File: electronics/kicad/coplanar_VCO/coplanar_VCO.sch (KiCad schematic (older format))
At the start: 22 parts, among them J1 CONN_01, J2 CONN_01, U1 HMC732, U2 CE3520K3

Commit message: Coplanar
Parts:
- removed C9: 100 nF, 0603, symbol SparkFun-Capacitors:4.7UF0603
- removed C?: 10 nF, 0402, symbol SparkFun-Capacitors:6PF-0402-50V-0.5%
- removed TPOP1: Voutput, TestPoint:TestPoint_Pad_1.0x1.0mm, symbol Connector:Test_Point
- added C10, C14, C15, C20, C24, C25, C29, C9: 0.1 uF, 0603, symbol SparkFun-Capacitors:0.1UF-0603-25V-5%
- added C11, C17, C19, C27, C31, C36, C?: 1 nF, 0402, symbol SparkFun-Capacitors:6PF-0402-50V-0.5%
- added C12, C28, C34: 1 nF, Resistor_SMD:R_0402_1005Metric, symbol SparkFun-Capacitors:4.7UF0603
- added C16, C30, C35, C?: 100 nF, 0603, symbol SparkFun-Capacitors:4.7UF0603
- added C18: 10 nF, 0402, symbol SparkFun-Capacitors:6PF-0402-50V-0.5%
- added C33: 10 nF, Resistor_SMD:R_0402_1005Metric, symbol SparkFun-Capacitors:4.7UF0603
- added C7: 100 pF, 0402, symbol SparkFun-Capacitors:6PF-0402-50V-0.5%
- added D1, D2, D3, D?: BAT15-04, Package_TO_SOT_SMD:SOT-23, symbol Diode:BAS40-04
- added L2: 220 nH, 0402, symbol SparkFun-Coils:INDUCTOR-0402-3.9NH
- added L3: 440 nH, Resistor_SMD:R_0402_1005Metric, symbol SparkFun-Coils:INDUCTOR-0402-3.9NH
- added P1: CONN_1, TestPoint:TestPoint_Pad_1.5x1.5mm, symbol conn:CONN_1
- added P2, P4, P8, P?: a, TestPoint:TestPoint_Pad_1.5x1.5mm, symbol conn:CONN_1
- added P3, P5, P6, P7: OUTPUT, Connector_PinHeader_2.54mm:PinHeader_1x01_P2.54mm_Vertical, symbol conn:CONN_1
- added R11, R13, R4, R8: 100, 0805, symbol SparkFun-Resistors:0.22OHM-0805-1_4W-1%
- added R12, R5: 50, 0805, symbol SparkFun-Resistors:0.22OHM-0805-1_4W-1%
- added R15, R18, R2, R7, R?: 10k, 0402, symbol SparkFun-Resistors:RESISTOR0402
- added R16, R9: 10k, Resistor_SMD:R_0402_1005Metric, symbol SparkFun-Resistors:RESISTOR0402
- added R3: PAT1220, 0xDBFB7:PAT1220, symbol 0xDBFB7:attenuator
- added R? (x4): 1k, Resistor_SMD:R_0603_1608Metric, symbol SparkFun-Resistors:RESISTOR0402
- added U1, U4, U5, U8, U9: SY100EP, Package_SO:SOIC-8_3.9x4.9mm_P1.27mm, symbol 0xDBFB7:SY100EP
- added U10: CE3520K3, 0xDBFB7:4-Micro-X, symbol 0xDBFB7:CE3520K3
- added U3: HMC363, Package_SO:SOIC-8-1EP_3.9x4.9mm_P1.27mm_EP2.35x2.35mm, symbol 0xDBFB7:HMC363
- added U6: SKY65013, Package_TO_SOT_SMD:SOT-89-3_Handsoldering, symbol 0xDBFB7:SKY65013
- C22: renamed from C10; value 1 nF -> 10 nF
- renumbered C8 to C13, C11 to C23, C12 to C26, C7 to C8, R2 to R10, U1 to U2, U2 to U7
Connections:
- net labels added: 3.3V, DIV8_OUT
- wire segments 11 -> 66
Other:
- note added: ""since the detector does not conserve phase information, all phasors that appear as factors can be replaced by their magnitudes." - *happiness noise*"
- note added: "Division of 8 * 4^5 = 8192\n1.464 MHz at 12 GHz."
- note added: "Input power range of the HMC. is max. +5 dBm across the spectrum, 0 dBm recommended.\n"
- note added: "O/P is -9 to -6 dBm, too low for the logic levels of the \nSY."
- note added: "RF diode detector based on infineon appnote AN_1807."
- note added: "Stub lengths < 7 mm probably don't need termination; see Shockman, termination.\nIn fact, the reflection overshoot will aid getting the signal levels between the thresholds."
- note added: "https://www.qsl.net/n9zia/pre1/index.html"
- moved on the sheet: C1, C13, C2, C22, C23, C26, C3, C4, C5, C6, C8, J1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

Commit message: coplanarizing further
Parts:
- removed C1: 10uF, 1206, symbol SparkFun-Capacitors:1.0UF-1206-50V-10%
- removed C10, C14, C15, C20, C24, C25, C29, C3, C9: 0.1 uF, 0603, symbol SparkFun-Capacitors:0.1UF-0603-25V-5%
- removed C11, C17, C19, C27, C36, C?: 1 nF, 0402, symbol SparkFun-Capacitors:6PF-0402-50V-0.5%
- removed C12, C28, C34: 1 nF, Resistor_SMD:R_0402_1005Metric, symbol SparkFun-Capacitors:4.7UF0603
- removed C13, C18: 10 nF, 0402, symbol SparkFun-Capacitors:6PF-0402-50V-0.5%
- removed C16, C35, C?: 100 nF, 0603, symbol SparkFun-Capacitors:4.7UF0603
- removed C26: 10 pF, Capacitor_SMD:C_0402_1005Metric, symbol SparkFun-Capacitors:6PF-0402-50V-0.5%
- removed C33: 10 nF, Resistor_SMD:R_0402_1005Metric, symbol SparkFun-Capacitors:4.7UF0603
- removed C7: 100 pF, 0402, symbol SparkFun-Capacitors:6PF-0402-50V-0.5%
- removed D1, D?: BAT15-04, Package_TO_SOT_SMD:SOT-23, symbol Diode:BAS40-04
- removed L2: 220 nH, 0402, symbol SparkFun-Coils:INDUCTOR-0402-3.9NH
- removed L3: 440 nH, Resistor_SMD:R_0402_1005Metric, symbol SparkFun-Coils:INDUCTOR-0402-3.9NH
- removed P2, P?: a, TestPoint:TestPoint_Pad_1.5x1.5mm, symbol conn:CONN_1
- removed P3: OUTPUT, Connector_PinHeader_2.54mm:PinHeader_1x01_P2.54mm_Vertical, symbol conn:CONN_1
- removed R11, R13, R4, R8: 100, 0805, symbol SparkFun-Resistors:0.22OHM-0805-1_4W-1%
- removed R12, R5: 50, 0805, symbol SparkFun-Resistors:0.22OHM-0805-1_4W-1%
- removed R16, R9: 10k, Resistor_SMD:R_0402_1005Metric, symbol SparkFun-Resistors:RESISTOR0402
- removed R18, R2, R7, R?: 10k, 0402, symbol SparkFun-Resistors:RESISTOR0402
- removed R3: PAT1220, 0xDBFB7:PAT1220, symbol 0xDBFB7:attenuator
- removed R? (x4): 1k, Resistor_SMD:R_0603_1608Metric, symbol SparkFun-Resistors:RESISTOR0402
- removed U1, U4, U5, U8, U9: SY100EP, Package_SO:SOIC-8_3.9x4.9mm_P1.27mm, symbol 0xDBFB7:SY100EP
- removed U10: CE3520K3, 0xDBFB7:4-Micro-X, symbol 0xDBFB7:CE3520K3
- removed U3: HMC363, Package_SO:SOIC-8-1EP_3.9x4.9mm_P1.27mm_EP2.35x2.35mm, symbol 0xDBFB7:HMC363
- removed U6: SKY65013, Package_TO_SOT_SMD:SOT-89-3_Handsoldering, symbol 0xDBFB7:SKY65013
- added C10, C12, C14, C15: 1 nF, Resistor_SMD:R_0402_1005Metric, symbol SparkFun-Capacitors:6PF-0402-50V-0.5%
- added C11, C9: 100 nF, 0603, symbol SparkFun-Capacitors:4.7UF0603
- added D4: BAT15-04, Package_TO_SOT_SMD:SOT-23, symbol Diode:BAS40-04
- added R3, R4, R5, R6, R8: 10k, Resistor_SMD:R_0402_1005Metric, symbol SparkFun-Resistors:RESISTOR0402
- C31, R15: footprint 0402 -> Resistor_SMD:R_0402_1005Metric
- C5, C6, C8: value 10 nF -> 1 nF
- L1: value 440 nH -> 220 nH
- P1: value CONN_1 -> a
- P5, P6, P7: value OUTPUT -> a; footprint Connector_PinHeader_2.54mm:PinHeader_1x01_P2.54mm_Vertical -> TestPoint:TestPoint_Pad_1.5x1.5mm
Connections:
- net labels removed: 3.3V, DIV8_OUT
- wire segments 66 -> 26
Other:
- note removed: "Division of 8 * 4^5 = 8192\n1.464 MHz at 12 GHz."
- note removed: "Input power range of the HMC. is max. +5 dBm across the spectrum, 0 dBm recommended.\n"
- note removed: "O/P is -9 to -6 dBm, too low for the logic levels of the \nSY."
- note removed: "https://www.qsl.net/n9zia/pre1/index.html"
- moved on the sheet: C2, C22, C23, C30, C31, C4, C5, C6, C8, D2, J1, J2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

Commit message: Coplanar
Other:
- moved on the sheet: TPSO1
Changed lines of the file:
@@
 L Connector:Test_Point TPSO1
 U 1 1 5F45EF57
-P 8500 900
-F 0 "TPSO1" H 8558 1018 50  0000 L CNN
-F 1 "Vsource" H 8558 927 50  0000 L CNN
-F 2 "TestPoint:TestPoint_Pad_1.0x1.0mm" H 8700 900 50  0001 C CNN
-F 3 "~" H 8700 900 50  0001 C CNN
-F 4 "V" H 8500 900 50  0001 C CNN "Spice_Primitive"
-F 5 "pulse(0 2 20p 5p 1p 1 1)" H 8500 900 50  0001 C CNN "Spice_Model"
-F 6 "N" H 8500 900 50  0001 C CNN "Spice_Netlist_Enabled"
-	1    8500 900
+P 3950 1650
+F 0 "TPSO1" H 4008 1768 50  0000 L CNN
+F 1 "Vsource" H 4008 1677 50  0000 L CNN
+F 2 "TestPoint:TestPoint_Pad_1.0x1.0mm" H 4150 1650 50  0001 C CNN
+F 3 "~" H 4150 1650 50  0001 C CNN
+F 4 "V" H 3950 1650 50  0001 C CNN "Spice_Primitive"
+F 5 "pulse(0 2 20p 5p 1p 1 1)" H 3950 1650 50  0001 C CNN "Spice_Model"
+F 6 "N" H 3950 1650 50  0001 C CNN "Spice_Netlist_Enabled"
+	1    3950 1650
 	1    0    0    -1
 $EndComp
-Text GLabel 8500 1050 2    50   Input ~ 0
+Text GLabel 3950 1800 2    50   Input ~ 0
 nsource
 Wire Wire Line
-	8500 900  8500 1050
+	3950 1650 3950 1800
 $Comp
 L SparkFun-Resistors:RESISTOR0402 R3

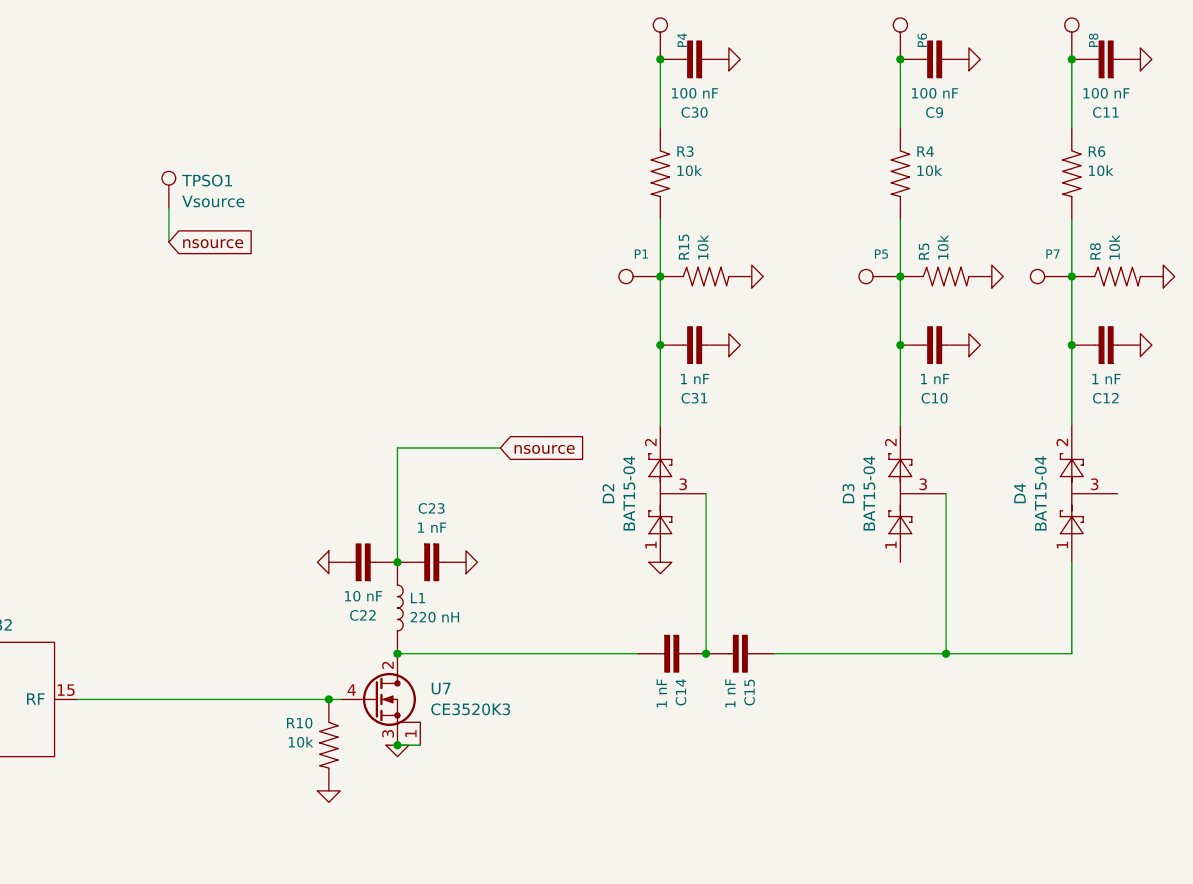
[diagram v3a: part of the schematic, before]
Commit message: integrated amp
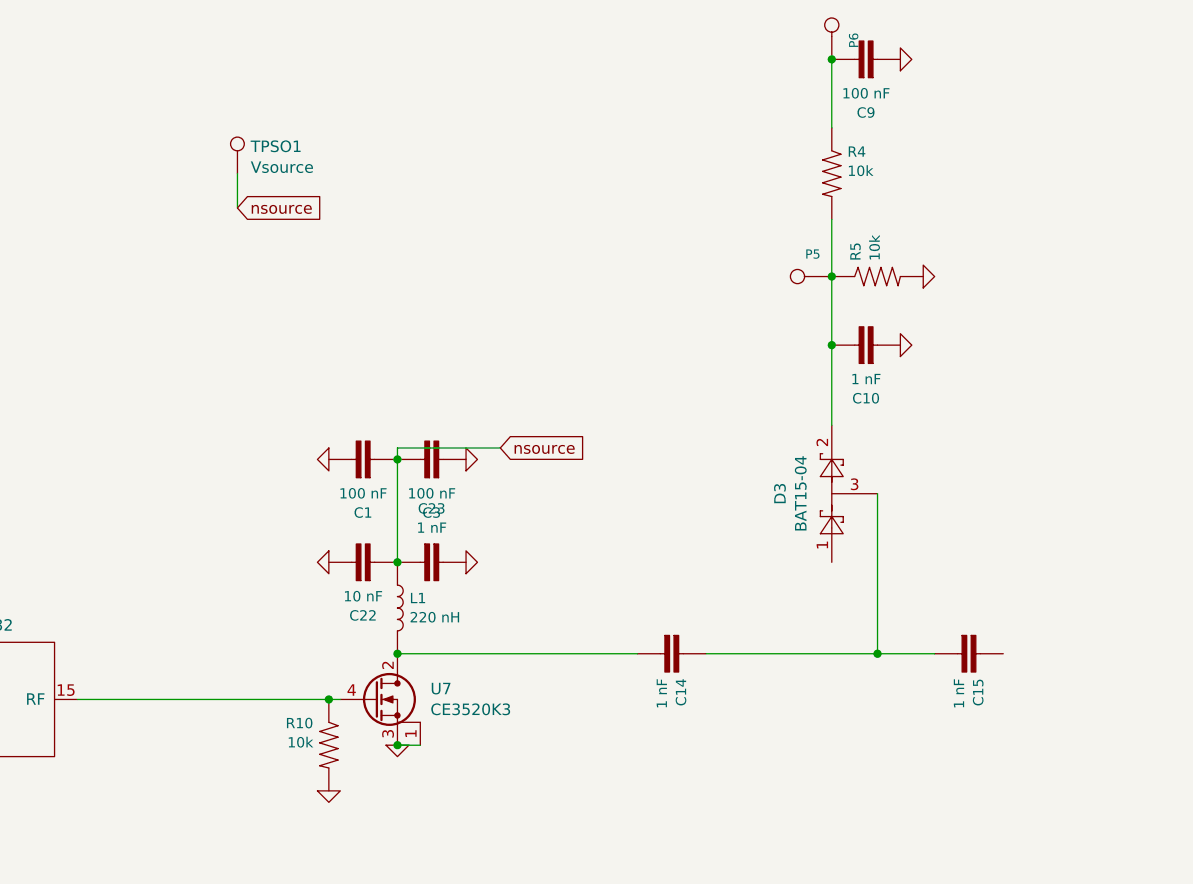
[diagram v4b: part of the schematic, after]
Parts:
- removed C11, C30: 100 nF, 0603, symbol SparkFun-Capacitors:4.7UF0603
- removed C12, C31: 1 nF, Resistor_SMD:R_0402_1005Metric, symbol SparkFun-Capacitors:6PF-0402-50V-0.5%
- removed D2, D4: BAT15-04, Package_TO_SOT_SMD:SOT-23, symbol Diode:BAS40-04
- removed P1, P4, P7, P8: a, TestPoint:TestPoint_Pad_1.5x1.5mm, symbol conn:CONN_1
- removed R15, R3, R6, R8: 10k, Resistor_SMD:R_0402_1005Metric, symbol SparkFun-Resistors:RESISTOR0402
- added C1, C3: 100 nF, 0603, symbol SparkFun-Capacitors:4.7UF0603
- J1: footprint TestPoint:TestPoint_Pad_1.5x1.5mm -> TestPoint:TestPoint_Pad_2.0x2.0mm
- TPSO1: footprint TestPoint:TestPoint_Pad_1.0x1.0mm -> TestPoint:TestPoint_Pad_2.5x2.5mm
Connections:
- net GND: now also C1.1, C3.2
- net nsource: now also C1.2, C3.1
- net at C14.1, C15.2: now also D3.3
- net at C15.1: no longer D3.3
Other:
- moved on the sheet: C10, C15, C9, D3, P5, P6, R4, R5, TPSO1
